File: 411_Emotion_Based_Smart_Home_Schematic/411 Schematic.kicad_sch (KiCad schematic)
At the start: 8 parts, among them Q1 NSS1C301ET4G, Q2 NSS1C301ET4G, Q3 NSS1C301ET4G, U4 HC-SR04

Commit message: Fixing Errors
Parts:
- added C1: 10u, symbol Device:C
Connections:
- net +9V: now also C1.1; no longer D1.1 (KB), D1.2 (KR), D1.3 (KG), D2.1 (KB), D2.2 (KR), D2.3 (KG), D3.1 (KB), D3.2 (KR), D3.3 (KG), Jetson 40-Pin1.14 (GND), Jetson 40-Pin1.20 (GND), Jetson 40-Pin1.25 (GND), Jetson 40-Pin1.30 (GND), Jetson 40-Pin1.34 (GND), Jetson 40-Pin1.39 (GND), Jetson 40-Pin1.6 (GND), Jetson 40-Pin1.9 (GND), U4.4 (GND)
- new net GND: C1.2, D1.1 (KB), D1.2 (KR), D1.3 (KG), D2.1 (KB), D2.2 (KR), D2.3 (KG), D3.1 (KB), D3.2 (KR), D3.3 (KG), Jetson 40-Pin1.14 (GND), Jetson 40-Pin1.20 (GND), Jetson 40-Pin1.25 (GND), Jetson 40-Pin1.30 (GND), Jetson 40-Pin1.34 (GND), Jetson 40-Pin1.39 (GND), Jetson 40-Pin1.6 (GND), Jetson 40-Pin1.9 (GND), U4.4 (GND)
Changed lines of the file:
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@@
 	(wire
 		(pts
-			(xy 86.36 85.09) (xy 86.36 101.6)
+			(xy 86.36 85.09) (xy 86.36 93.98)
 		)
 		(stroke
@@
 					(unit 1)
 				)
+			)
+		)
+	)
+	(symbol
+		(lib_id "Device:C")
+		(at 86.36 97.79 0)
+		(unit 1)
+		(exclude_from_sim no)
+		(in_bom yes)
+		(on_board yes)
+		(dnp no)
+		(fields_autoplaced yes)
+		(property "Reference" "C1"
+			(at 90.17 96.5199 0)
+			(effects
+				(font
+					(size 1.27 1.27)
+				)
+				(justify left)
+			)
+		)
+		(property "Value" "10u"
+			(at 90.17 99.0599 0)
+			(effects
+				(font
+					(size 1.27 1.27)
+				)
+				(justify left)
+			)
+		)
+		(property "Footprint" ""
+			(at 87.3252 101.6 0)
+			(effects
+				(font
+					(size 1.27 1.27)
+				)
+				(hide yes)
+			)
+		)
+		(property "Datasheet" "~"
+			(at 86.36 97.79 0)
+			(effects
+				(font
+					(size 1.27 1.27)
+				)
+				(hide yes)
+			)
+		)
+		(property "Description" "Unpolarized capacitor"
+			(at 86.36 97.79 0)
+			(effects
+				(font
+					(size 1.27 1.27)
+				)
+				(hide yes)
+			)
+		)
+		(pin "2"
+		)
+		(pin "1"
+		)
+		(instances
+			(project ""
+				(path "/5dc6eed7-92e4-45e8-95d9-22a5fc08946e"
+					(reference "C1")
+					(unit 1)
+				)

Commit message: PCB Rough route and schematic almost finished
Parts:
- Jetson_40-Pin1: renamed from Jetson 40-Pin1; footprint (none) -> Connector_PinHeader_2.54mm:PinHeader_2x40_P2.54mm_Vertical
- Q1, Q2, Q3: footprint (none) -> Transistor411Library:DPAK-4_6P22X6P73_ONS
- U4: footprint HC-SR04:XCVR_HC-SR04 -> Connector_PinSocket_2.54mm:PinSocket_1x04_P2.54mm_Vertical
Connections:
- net 3.3V renamed 5V
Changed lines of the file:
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@@
 		)
 	)
-	(label "3.3V"
+	(label "5V"
 		(at 138.43 41.91 0)
 		(fields_autoplaced yes)
@@
 		(dnp no)
 		(fields_autoplaced yes)
-		(property "Reference" "Jetson 40-Pin1"
+		(property "Reference" "Jetson_40-Pin1"
 			(at 179.07 78.74 0)
 			(effects
@@
 			)
 		)
-		(property "Footprint" ""
+		(property "Footprint" "Connector_PinHeader_2.54mm:PinHeader_2x40_P2.54mm_Vertical"
 			(at 179.07 123.19 0)
 			(effects
@@
 			(project ""
 				(path "/5dc6eed7-92e4-45e8-95d9-22a5fc08946e"
-					(reference "Jetson 40-Pin1")
+					(reference "Jetson_40-Pin1")
 					(unit 1)
 				)
@@
 			)
 		)
-		(property "Footprint" ""
+		(property "Footprint" "Transistor411Library:DPAK-4_6P22X6P73_ONS"
 			(at 52.07 132.08 0)
 			(effects
@@
 			)
 		)
-		(property "Footprint" "HC-SR04:XCVR_HC-SR04"
+		(property "Footprint" "Connector_PinSocket_2.54mm:PinSocket_1x04_P2.54mm_Vertical"
 			(at 173.99 44.45 0)
 			(effects
@@
 			)
 		)
-		(property "Footprint" ""
+		(property "Footprint" "Transistor411Library:DPAK-4_6P22X6P73_ONS"
 			(at 73.66 132.08 0)
 			(effects
@@
 			)
 		)
-		(property "Footprint" ""
+		(property "Footprint" "Transistor411Library:DPAK-4_6P22X6P73_ONS"
 			(at 92.71 132.08 0)
 			(effects

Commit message: Updated schematic.
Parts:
- removed C1: 10u, symbol Device:C
- removed D1, D2, D3: Inolux_IN-P55TATRGB, LED_SMD:LED_Inolux_IN-P55TATRGB_PLCC6_5.0x5.5mm_P1.8mm, symbol LED:Inolux_IN-P55TATRGB
- added D1, D2, D4: LED_RGB, LED_SMD:LED_RGB_5050-6, symbol Device:LED_RGB
- added R1, R2, R3: 10, Resistor_THT:R_Axial_DIN0411_L9.9mm_D3.6mm_P5.08mm_Vertical, symbol Device:R_Small_US
- Q1, Q2, Q3: footprint Transistor411Library:DPAK-4_6P22X6P73_ONS -> NSS1C301ET4G:DPAK-4_6P22X6P73_ONS
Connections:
- net 5V: now also Q1.2 (C), Q2.2 (C), Q3.2 (C)
- net GND: now also D1.1 (RK), D1.2 (GK), D1.3 (BK), D2.1 (RK), D2.2 (GK), D2.3 (BK), D4.1 (RK), D4.2 (GK), D4.3 (BK); no longer Jetson_40-Pin1.14 (GND), Jetson_40-Pin1.20 (GND), Jetson_40-Pin1.25 (GND), Jetson_40-Pin1.30 (GND), Jetson_40-Pin1.34 (GND), Jetson_40-Pin1.6 (GND), Jetson_40-Pin1.9 (GND), U4.4 (GND)
- net Q1: now also D1.5 (GA), D2.5 (GA), D4.5 (GA), R3.1; no longer Q1.3 (E)
- net Q2: now also D1.4 (BA), D2.4 (BA), D4.4 (BA), R2.1; no longer Q2.3 (E)
- net Q3: now also D1.6 (RA), D2.6 (RA), D4.6 (RA), R1.1; no longer Q3.3 (E)
- net at Jetson_40-Pin1.10 (UART1_RXD): no longer U4.3 (ECHO)
- net at Jetson_40-Pin1.15 (GPIO12): now also U4.3 (ECHO)
- new net: Jetson_40-Pin1.9 (GND), U4.4 (GND)
- new net: Q2.3 (E), R2.2
- new net: Q3.3 (E), R1.2
- new net: Q1.3 (E), R3.2
- now unconnected: Jetson_40-Pin1.1 (3.3V)
- no-connect marks 25 -> 1
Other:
- note added: "Blue_LED_ON"
- note added: "Green_LED_ON"
- note added: "Red_LED_ON"
- note removed: "Blue_ON"
- note removed: "Green_ON"
- note removed: "Power"
- note removed: "Red_ON"
- note removed: "This is the power from the outlet, powering the jetson nano"
- moved on the sheet: Q1, Q2, Q3

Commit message: Updated schematic.
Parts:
- added R4, R5, R6: 10k, Resistor_THT:R_Axial_DIN0411_L9.9mm_D3.6mm_P5.08mm_Vertical, symbol Device:R_Small_US
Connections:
- net at Jetson_40-Pin1.1 (3.3V): now also R4.1, R5.1, R6.1
- net at Jetson_40-Pin1.29 (GPIO01), Q3.1 (B): now also R5.2
- net at Jetson_40-Pin1.31 (GPIO11), Q2.1 (B): now also R4.2
- net at Jetson_40-Pin1.33 (GPIO13), Q1.1 (B): now also R6.2
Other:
- note added: "LED 5V"
- note removed: "LED 3.3V"
- moved on the sheet: D1, D2, D4

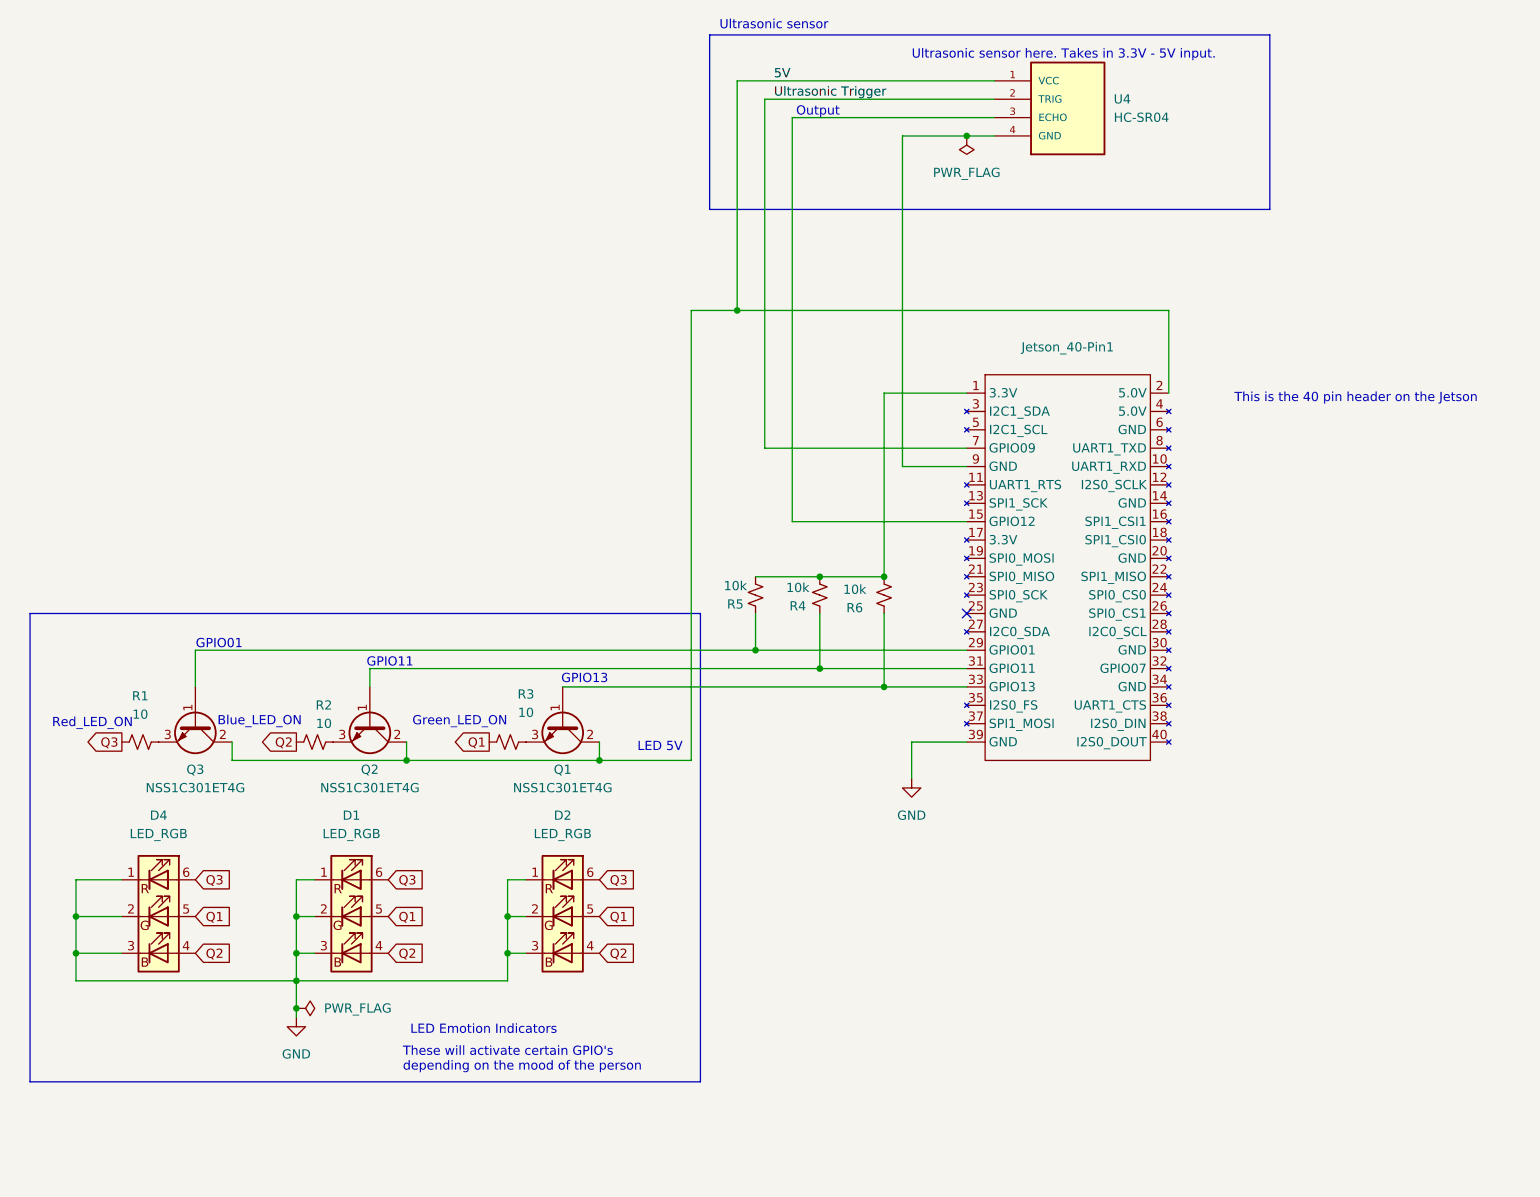
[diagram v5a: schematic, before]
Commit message: Added TP and cleaned up all the traces.
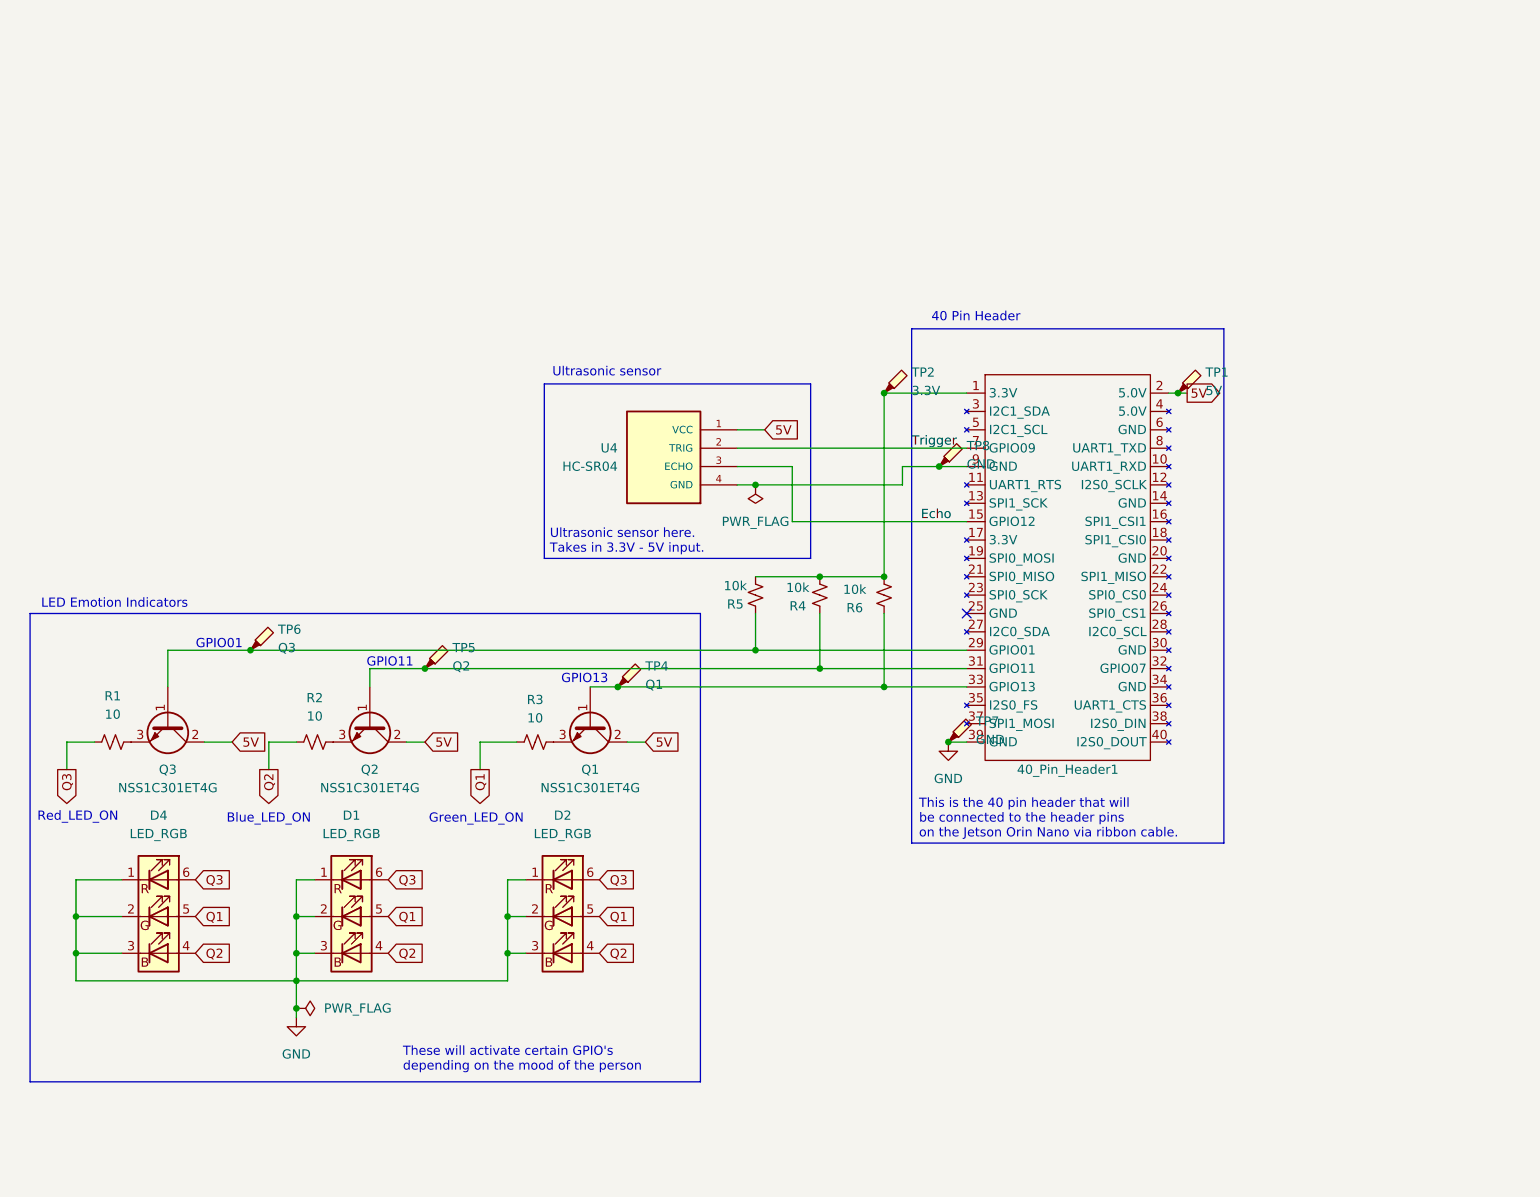
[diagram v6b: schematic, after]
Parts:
- added TP1: 5V, TestPoint:TestPoint_Pad_1.0x1.0mm, symbol Connector:TestPoint_Probe
- added TP2: 3.3V, TestPoint:TestPoint_Pad_1.0x1.0mm, symbol Connector:TestPoint_Probe
- added TP4: Q1, TestPoint:TestPoint_Pad_1.0x1.0mm, symbol Connector:TestPoint_Probe
- added TP5: Q2, TestPoint:TestPoint_Pad_1.0x1.0mm, symbol Connector:TestPoint_Probe
- added TP6: Q3, TestPoint:TestPoint_Pad_1.0x1.0mm, symbol Connector:TestPoint_Probe
- added TP7, TP8: GND, TestPoint:TestPoint_Pad_1.0x1.0mm, symbol Connector:TestPoint_Probe
- renumbered Jetson_40-Pin1 to 40_Pin_Header1
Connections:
- net 5V: now also TP1.1
- net GND: now also TP7.1
- net at 40_Pin_Header1.1 (3.3V), R4.1, R5.1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: now also TP2.1
- net Echo: now reaches 40_Pin_Header1.15 (GPIO12), U4.3 (ECHO)
- net at 40_Pin_Header1.29 (GPIO01), Q3.1 (B), R5.2: now also TP6.1
- net at 40_Pin_Header1.31 (GPIO11), Q2.1 (B), R4.2: now also TP5.1
- net at 40_Pin_Header1.33 (GPIO13), Q1.1 (B), R6.2: now also TP4.1
- net at 40_Pin_Header1.9 (GND), U4.4 (GND): now also TP8.1
- net Ultrasonic Trigger renamed Trigger
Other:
- note added: "40 Pin Header"
- note added: "This is the 40 pin header that will be connected to the header pins on the Jetson Orin Nano via ribbon cable."
- note removed: "LED 5V"
- note removed: "Output"
- note removed: "This is the 40 pin header on the Jetson"
- moved on the sheet: Q1, Q3, R1, R3, U4

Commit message: Updated schematic and layout.
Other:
- note added: "Pull-up resistors."
- note added: "Takes in 3.3V - 5V input."
- note added: "These will turn on based on GPIO's signal depending on the mood of the person."
- note added: "This is the 40 pin header that will be connected to the header pins on the Jetson Orin Nano via ribbon cable. The Jetson will provide power as well as the signal from the GPIO."
- note removed: "These will activate certain GPIO's depending on the mood of the person"
- note removed: "This is the 40 pin header that will be connected to the header pins on the Jetson Orin Nano via ribbon cable."
- note removed: "Ultrasonic sensor here. Takes in 3.3V - 5V input."
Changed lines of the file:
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@@
 	(title_block
 		(title "Emotion-Adaptive-Smart-Home")
-		(date "2024-11-06")
+		(date "2024-11-20")
 		(rev "4")
 		(company "411 Group 6")
@@
 	)
 	(rectangle
-		(start 157.48 76.2)
-		(end 200.66 147.32)
+		(start 130.81 109.22)
+		(end 156.21 118.11)
 		(stroke
 			(width 0)
@@
 		)
 	)
-	(text "GPIO11"
-		(exclude_from_sim no)
-		(at 85.344 122.428 0)
+	(rectangle
+		(start 157.48 76.2)
+		(end 200.66 151.13)
+		(stroke
+			(width 0)
+			(type default)
+		)
+		(fill
+			(type none)
+		)
+	)
+	(text "Pull-up resistors."
+		(exclude_from_sim no)
+		(at 139.446 119.38 0)
 		(effects
 			(font
@@
 		)
 	)
-	(text "GPIO13"
-		(exclude_from_sim no)
-		(at 112.268 124.714 0)
+	(text "GPIO11"
+		(exclude_from_sim no)
+		(at 85.344 122.428 0)
 		(effects
 			(font
@@
 		)
 	)
-	(text "This is the 40 pin header that will \nbe connected to the header pins \non the Jetson Orin Nano via ribbon cable.\n"
-		(exclude_from_sim no)
-		(at 158.496 144.018 0)
+	(text "GPIO13"
+		(exclude_from_sim no)
+		(at 112.268 124.714 0)
+		(effects
+			(font
+				(size 1.27 1.27)
+			)
+		)
+	)
+	(text "This is the 40 pin header that will \nbe connected to the header pins \non the Jetson Orin Nano via ribbon cable.\nThe Jetson will provide power as well as \nthe signal from the GPIO.\n"
+		(exclude_from_sim no)
+		(at 158.242 145.542 0)
 		(effects
 			(font
@@
 		)
 	)
-	(text "Ultrasonic sensor here. \nTakes in 3.3V - 5V input."
+	(text "Takes in 3.3V - 5V input."
 		(exclude_from_sim no)
 		(at 107.442 105.664 0)
@@
 		)
 	)
-	(text "These will activate certain GPIO's\ndepending on the mood of the person"
-		(exclude_from_sim no)
-		(at 87.122 177.292 0)
-		(effects
-			(font
+	(text "These will turn on based on GPIO's signal\ndepending on the mood of the person."
+		(exclude_from_sim no)
+		(at 85.09 177.292 0)
+		(effects
+			(font
